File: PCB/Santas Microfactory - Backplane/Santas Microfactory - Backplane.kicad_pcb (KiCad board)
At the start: 2 copper layers, 100.2 x 102 mm, 13 parts, among them CN1 2EG08217-D2D-DF, CN2 2EG08217-D2D-DF, CN3 2EG08217-D2D-DF, CN4 2EG08217-D2D-DF, CN5 2EG08217-D2D-DF, CN6 2EG08217-D2D-DF, CN7 2EG08217-D2D-DF

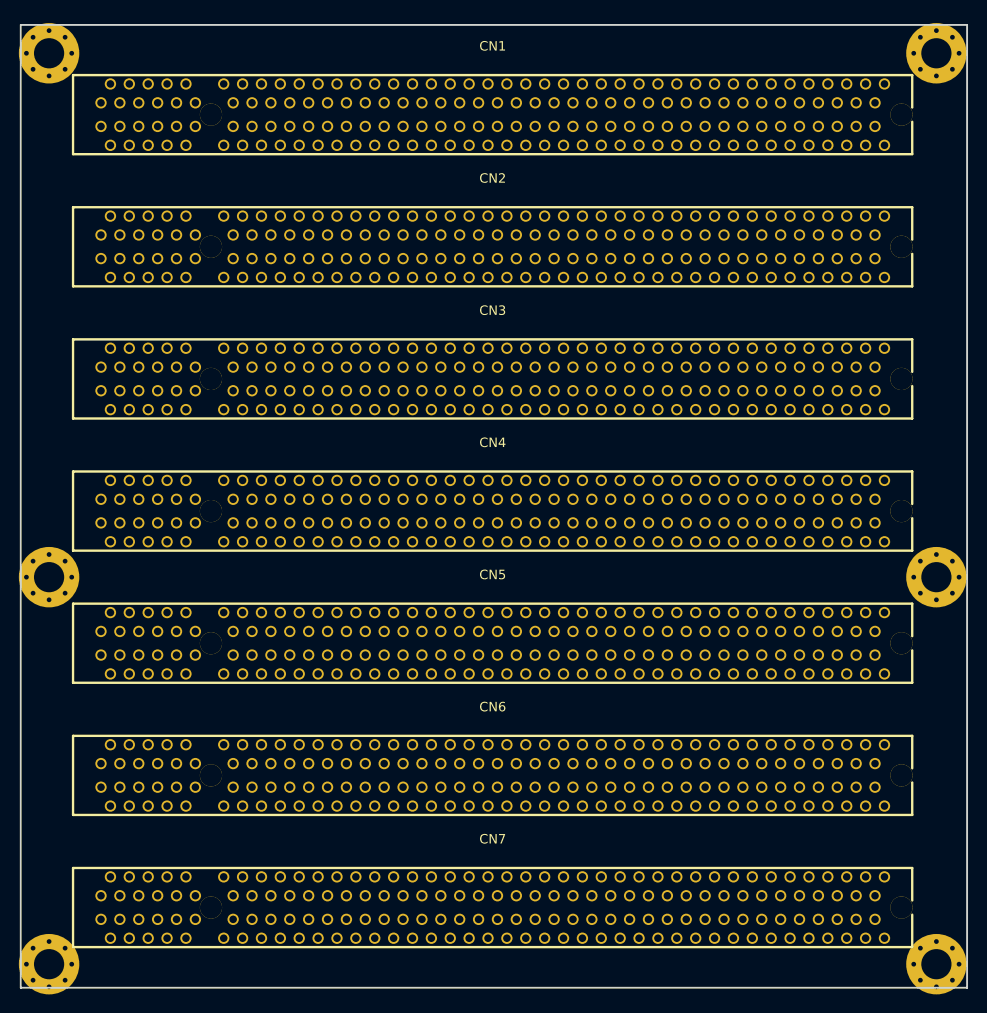
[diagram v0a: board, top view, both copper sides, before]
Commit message: Finished Backplane
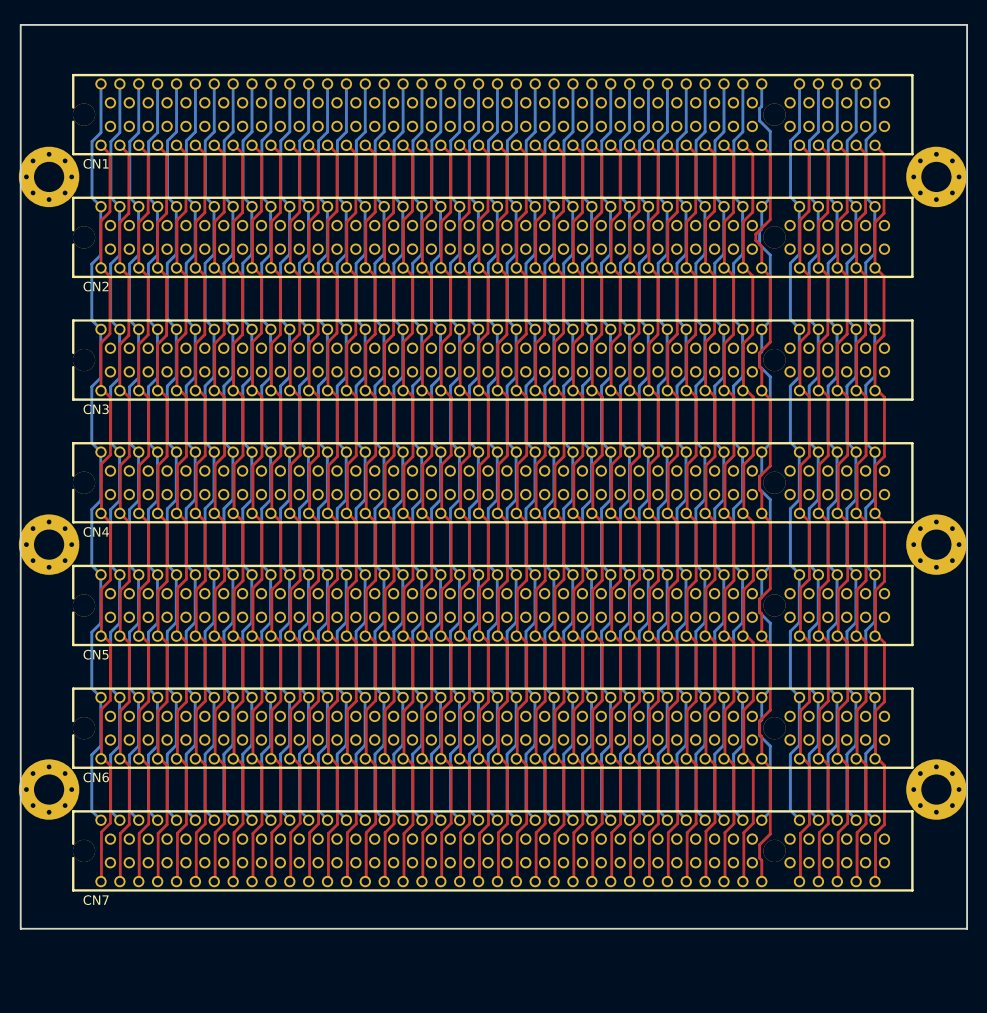
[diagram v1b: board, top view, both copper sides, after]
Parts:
- moved H3 18.5 mm to (53.0, 121.5)
- moved H6 18.5 mm to (147.0, 121.5)
- moved H1 13.1 mm to (53.0, 56.6)
- moved H5 13.1 mm to (147.0, 56.6)
- moved CN7 6.00 mm to (100.0, 128.0), turned to 180 degrees
- moved CN6 5.00 mm to (100.0, 115.0), turned to 180 degrees
- moved CN5 4.00 mm to (100.0, 102.0), turned to 180 degrees
- moved H2 3.45 mm to (53.0, 95.6)
- moved H4 3.45 mm to (147.0, 95.6)
- moved CN4 3.00 mm to (100.0, 89.0), turned to 180 degrees
- moved CN3 2.00 mm to (100.0, 76.0), turned to 180 degrees
- moved CN2 1.00 mm to (100.0, 63.0), turned to 180 degrees
- turned CN1 to 180 degrees
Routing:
- net A12: track 0.00 -> 83.9 mm
- net B12: track 0.00 -> 83.6 mm
- net B43: track 0.00 -> 83.2 mm
- net B67: track 0.00 -> 83.2 mm
- net B35: track 0.00 -> 83.2 mm
- net B27: track 0.00 -> 83.2 mm
- net B75: track 0.00 -> 83.2 mm
- net B59: track 0.00 -> 83.2 mm
- net B51: track 0.00 -> 83.2 mm
- net B5: track 0.00 -> 83.2 mm
- net B19: track 0.00 -> 83.2 mm
- net B77: track 0.00 -> 83.0 mm
- net B29: track 0.00 -> 83.0 mm
- net A62: track 0.00 -> 83.0 mm
- net B7: track 0.00 -> 83.0 mm
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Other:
- board size 100.2 x 102 mm -> 100.2 x 95.8 mm
- copper layers 2 -> 4

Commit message: All silkscreen additions + Gerbers and CAD files
Silkscreen and Gerbers are done, but I plan on using the CAD to create additional renders.
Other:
- board text added: "Making"
- board text added: "Sand"
- board text added: "Santas Microfactory"
- board text added: "Think"
